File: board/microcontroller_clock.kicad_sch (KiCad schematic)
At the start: 3 parts, among them Y301 32768Hz

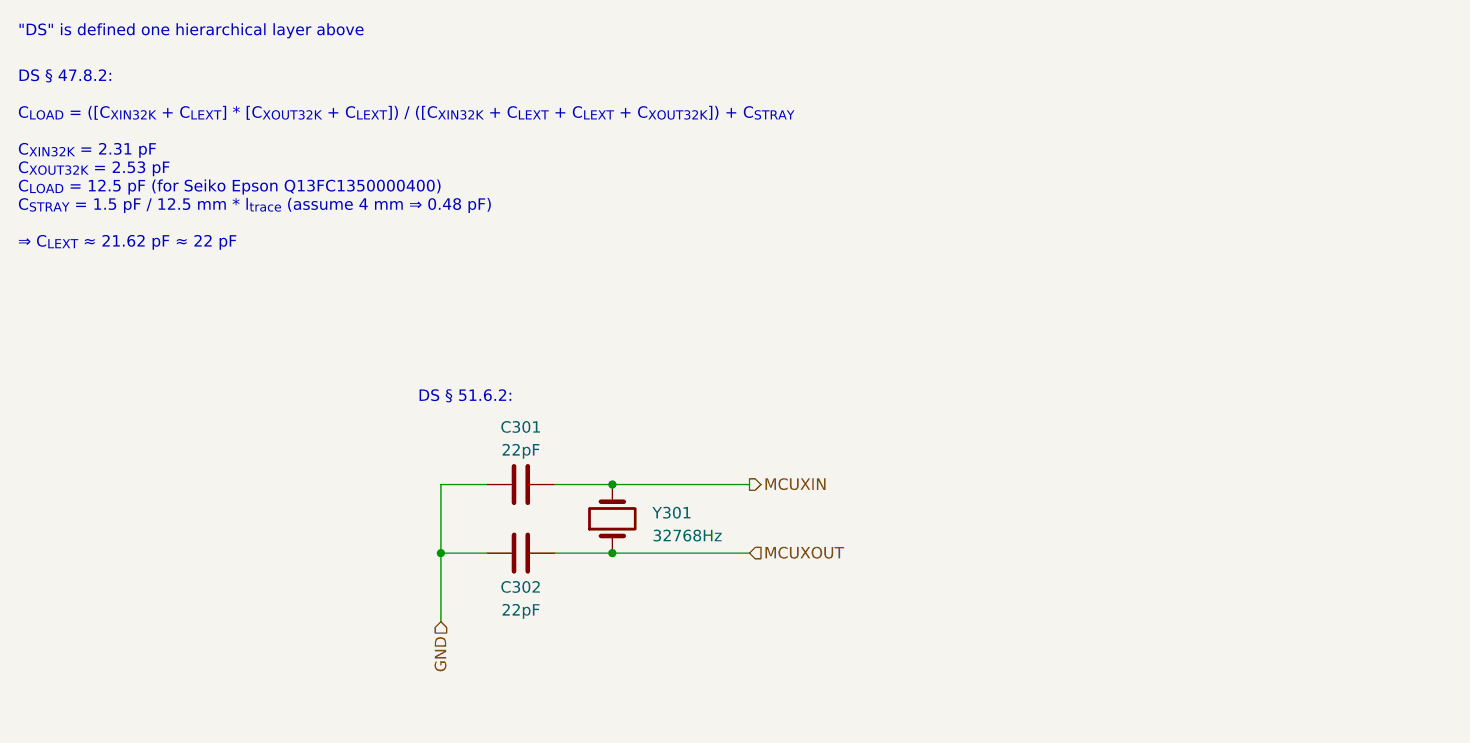
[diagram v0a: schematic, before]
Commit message: redo board with STM32G0B0CET
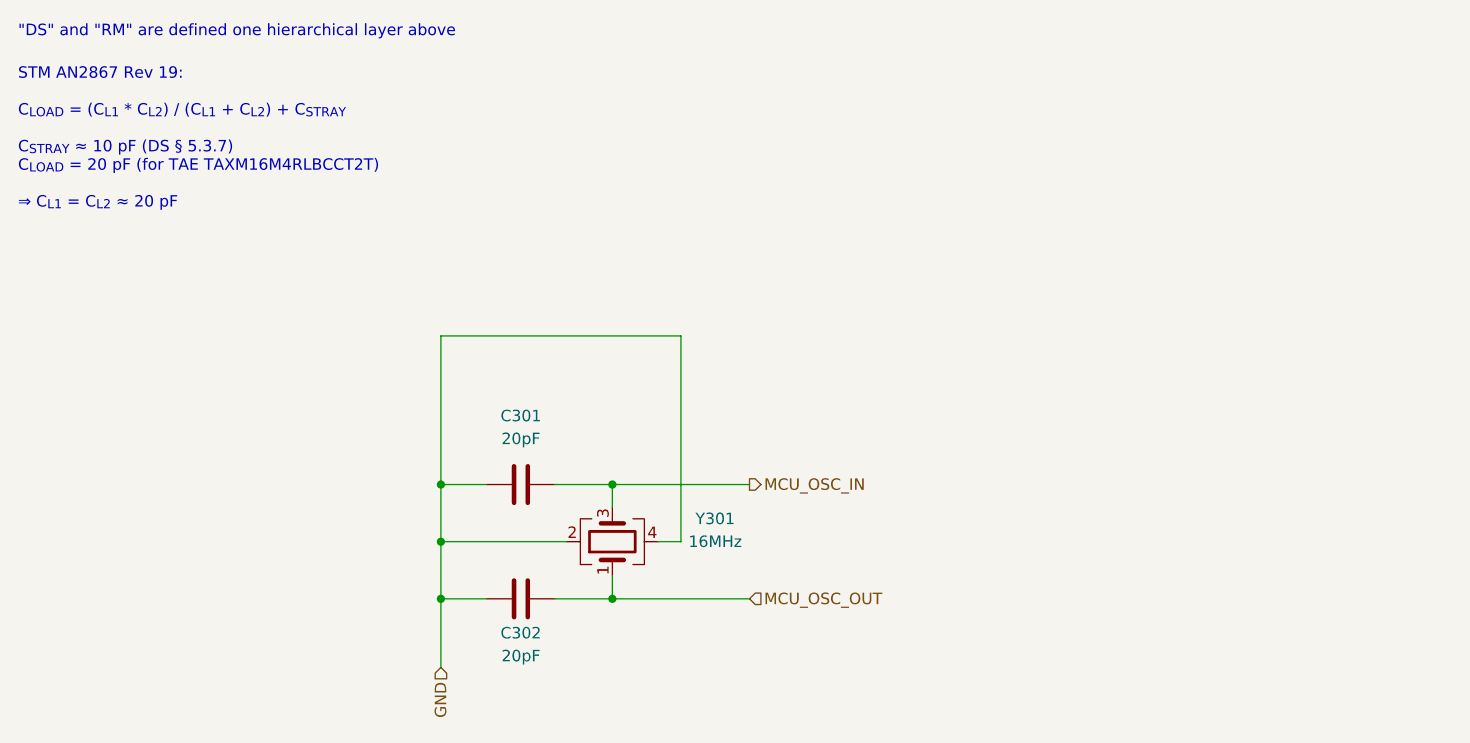
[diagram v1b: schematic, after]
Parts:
- C301, C302: value 22pF -> 20pF; LCSC C1555 -> C1554
- Y301: value 32768Hz -> 16MHz; footprint Crystal:Crystal_SMD_3215-2Pin_3.2x1.5mm -> Crystal:Crystal_SMD_3225-4Pin_3.2x2.5mm; symbol Device:Crystal -> Device:Crystal_GND24; LCSC C5120559 -> C164049
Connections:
- net GND: now also Y301.2, Y301.4
- net MCUXIN renamed MCU_OSC_IN
- net MCU_OSC_IN: now also Y301.3; no longer Y301.2
- net MCUXOUT renamed MCU_OSC_OUT
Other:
- note added: ""DS" and "RM" are defined one hierarchical layer above"
- note added: "STM AN2867 Rev 19: C_{LOAD} = (C_{L1} * C_{L2}) / (C_{L1} + C_{L2}) + C_{STRAY} C_{STRAY} ≈ 10 pF (DS § 5.3.7) C_{LOAD} = 20 pF (for TAE TAXM16M4RLBCCT2T) ⇒ C_{L1} = C_{L2} ≈ 20 pF"
- note removed: ""DS" is defined one hierarchical layer above"
- note removed: "DS § 47.8.2: C_{LOAD} = ([C_{XIN32K} + C_{LEXT}] * [C_{XOUT32K} + C_{LEXT}]) / ([C_{XIN32K} + C_{LEXT} + C_{LEXT} + C_{XOUT32K}]) + C_{STRAY} C_{XIN32K} = 2.31 pF C_{XOUT32K} = 2.53 pF C_{LOAD} = 12.5 pF (for Seiko Epson Q13FC1350000400) C_{STRAY} = 1.5 pF / 12.5 mm * l_{trace} (assume 4 mm ⇒ 0.48 pF) ⇒ C_{LEXT} ≈ 21.62 pF ≈ 22 pF"
- note removed: "DS § 51.6.2:"
- moved on the sheet: C302
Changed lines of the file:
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@@
 (kicad_sch (version 20230121) (generator eeschema)
   (paper "A4")
-  (junction (at 60.96 72.39) (diameter 0) (color 0 0 0 0)
+  (junction (at 60.96 77.47) (diameter 0) (color 0 0 0 0)
+  )
+  (junction (at 60.96 71.12) (diameter 0) (color 0 0 0 0)
   )
   (junction (at 80.01 64.77) (diameter 0) (color 0 0 0 0)
   )
-  (junction (at 80.01 72.39) (diameter 0) (color 0 0 0 0)
+  (junction (at 80.01 77.47) (diameter 0) (color 0 0 0 0)
+  )
+  (junction (at 60.96 64.77) (diameter 0) (color 0 0 0 0)
+  )
+  (wire (pts (xy 60.96 48.26) (xy 60.96 64.77))
+    (stroke (width 0) (type default))
+  )
+  (wire (pts (xy 60.96 71.12) (xy 60.96 77.47))
+    (stroke (width 0) (type default))
+  )
+  (wire (pts (xy 60.96 71.12) (xy 74.93 71.12))
+    (stroke (width 0) (type default))
+  )
+  (wire (pts (xy 87.63 71.12) (xy 85.09 71.12))
+    (stroke (width 0) (type default))
   )
   (wire (pts (xy 80.01 64.77) (xy 95.25 64.77))
     (stroke (width 0) (type default))
   )
-  (wire (pts (xy 60.96 72.39) (xy 60.96 80.01))
+  (wire (pts (xy 80.01 67.31) (xy 80.01 64.77))
     (stroke (width 0) (type default))
   )
-  (wire (pts (xy 73.66 72.39) (xy 80.01 72.39))
+  (wire (pts (xy 87.63 71.12) (xy 87.63 48.26))
     (stroke (width 0) (type default))
   )
-  (wire (pts (xy 80.01 72.39) (xy 95.25 72.39))
+  (wire (pts (xy 60.96 77.47) (xy 60.96 85.09))
     (stroke (width 0) (type default))
   )
-  (wire (pts (xy 60.96 72.39) (xy 66.04 72.39))
+  (wire (pts (xy 87.63 48.26) (xy 60.96 48.26))
+    (stroke (width 0) (type default))
+  )
+  (wire (pts (xy 73.66 77.47) (xy 80.01 77.47))
+    (stroke (width 0) (type default))
+  )
+  (wire (pts (xy 80.01 77.47) (xy 80.01 74.93))
+    (stroke (width 0) (type default))
+  )
+  (wire (pts (xy 80.01 77.47) (xy 95.25 77.47))
+    (stroke (width 0) (type default))
+  )
+  (wire (pts (xy 60.96 77.47) (xy 66.04 77.47))
     (stroke (width 0) (type default))
   )
@@
     (stroke (width 0) (type default))
   )
-  (wire (pts (xy 60.96 64.77) (xy 60.96 72.39))
+  (wire (pts (xy 60.96 64.77) (xy 60.96 71.12))
     (stroke (width 0) (type default))
   )
-  (text "DS § 51.6.2:" (at 58.42 55.88 0)
+  (text "STM AN2867 Rev 19:\n\nC_{LOAD} = (C_{L1} * C_{L2}) / (C_{L1} + C_{L2}) + C_{STRAY}\n\nC_{STRAY} ≈ 10 pF (DS § 5.3.7)\nC_{LOAD} = 20 pF (for TAE TAXM16M4RLBCCT2T)\n\n⇒ C_{L1} = C_{L2} ≈ 20 pF"
+    (at 13.97 34.29 0)
     (effects (font (size 1.27 1.27)) (justify left bottom))
   )
-  (text "DS § 47.8.2:\n\nC_{LOAD} = ([C_{XIN32K} + C_{LEXT}] * [C_{XOUT32K} + C_{LEXT}]) / ([C_{XIN32K} + C_{LEXT} + C_{LEXT} + C_{XOUT32K}]) + C_{STRAY}\n\nC_{XIN32K} = 2.31 pF\nC_{XOUT32K} = 2.53 pF\nC_{LOAD} = 12.5 pF (for Seiko Epson Q13FC1350000400)\nC_{STRAY} = 1.5 pF / 12.5 mm * l_{trace} (assume 4 mm ⇒ 0.48 pF)\n\n⇒ C_{LEXT} ≈ 21.62 pF ≈ 22 pF"
-    (at 13.97 38.735 0)
+  (text "\"DS\" and \"RM\" are defined one hierarchical layer above"
+    (at 13.97 15.24 0)
     (effects (font (size 1.27 1.27)) (justify left bottom))
   )
-  (text "\"DS\" is defined one hierarchical layer above" (at 13.97 15.24 0)
-    (effects (font (size 1.27 1.27)) (justify left bottom))
-  )
-  (hierarchical_label "MCUXIN" (shape output) (at 95.25 64.77 0) (fields_autoplaced)
+  (hierarchical_label "MCU_OSC_IN" (shape output) (at 95.25 64.77 0) (fields_autoplaced)
     (effects (font (size 1.27 1.27)) (justify left))
   )
-  (hierarchical_label "MCUXOUT" (shape input) (at 95.25 72.39 0) (fields_autoplaced)
+  (hierarchical_label "MCU_OSC_OUT" (shape input) (at 95.25 77.47 0) (fields_autoplaced)
     (effects (font (size 1.27 1.27)) (justify left))
   )
-  (hierarchical_label "GND" (shape input) (at 60.96 80.01 270) (fields_autoplaced)
+  (hierarchical_label "GND" (shape input) (at 60.96 85.09 270) (fields_autoplaced)
     (effects (font (size 1.27 1.27)) (justify right))
   )
-  (symbol (lib_id "Device:Crystal") (at 80.01 68.58 90) (unit 1)
-    (in_bom yes) (on_board yes) (dnp no) (fields_autoplaced)
-    (property "Reference" "Y301" (at 84.455 67.945 90)
-      (effects (font (size 1.27 1.27)) (justify right))
+  (symbol (lib_id "Device:Crystal_GND24") (at 80.01 71.12 90) (unit 1)
+    (in_bom yes) (on_board yes) (dnp no)
+    (property "Reference" "Y301" (at 91.44 68.58 90)
+      (effects (font (size 1.27 1.27)))
     )
-    (property "Value" "32768Hz" (at 84.455 70.485 90)
-      (effects (font (size 1.27 1.27)) (justify right))
+    (property "Value" "16MHz" (at 91.44 71.12 90)
+      (effects (font (size 1.27 1.27)))
     )
-    (property "Footprint" "Crystal:Crystal_SMD_3215-2Pin_3.2x1.5mm" (at 80.01 68.58 0)
+    (property "Footprint" "Crystal:Crystal_SMD_3225-4Pin_3.2x2.5mm" (at 80.01 71.12 0)
       (effects (font (size 1.27 1.27)) hide)
     )
-    (property "Datasheet" "~" (at 80.01 68.58 0)
+    (property "Datasheet" "~" (at 80.01 71.12 0)
       (effects (font (size 1.27 1.27)) hide)
     )
-    (property "LCSC" "C5120559" (at 80.01 68.58 0)
+    (property "LCSC" "C164049" (at 80.01 71.12 0)
       (effects (font (size 1.27 1.27)) hide)
     )
     (pin "1")
     (pin "2")
+    (pin "3")
+    (pin "4")
     (instances
       (project "bigredbutton"
@@
       )
       (project "enocean-heater-control"
-        (path "/5b6b7d93-1453-4f42-9207-d781d45a3d31/6e36ffc7-833c-490a-a419-d98d15ce7ac1/3e07dc11-3721-40d9-b0d4-7cbd77bafa21"
+        (path "/5b6b7d93-1453-4f42-9207-d781d45a3d31/6e36ffc7-833c-490a-a419-d98d15ce7ac1/ffec0bb5-2308-4547-a917-e412ae73decd"
           (reference "Y301") (unit 1)
         )
@@
   (symbol (lib_id "Device:C") (at 69.85 64.77 270) (unit 1)
     (in_bom yes) (on_board yes) (dnp no) (fields_autoplaced)
-    (property "Reference" "C301" (at 69.85 58.42 90)
+    (property "Reference" "C301" (at 69.85 57.15 90)
       (effects (font (size 1.27 1.27)))
     )
-    (property "Value" "22pF" (at 69.85 60.96 90)
+    (property "Value" "20pF" (at 69.85 59.69 90)
       (effects (font (size 1.27 1.27)))
     )
@@
       (effects (font (size 1.27 1.27)) hide)
     )
-    (property "LCSC" "C1555" (at 69.85 64.77 0)
+    (property "LCSC" "C1554" (at 69.85 64.77 0)
       (effects (font (size 1.27 1.27)) hide)
     )
@@
       )
       (project "enocean-heater-control"
-        (path "/5b6b7d93-1453-4f42-9207-d781d45a3d31/6e36ffc7-833c-490a-a419-d98d15ce7ac1/3e07dc11-3721-40d9-b0d4-7cbd77bafa21"
+        (path "/5b6b7d93-1453-4f42-9207-d781d45a3d31/6e36ffc7-833c-490a-a419-d98d15ce7ac1/ffec0bb5-2308-4547-a917-e412ae73decd"
           (reference "C301") (unit 1)
         )
@@
     )
   )
-  (symbol (lib_id "Device:C") (at 69.85 72.39 90) (unit 1)
+  (symbol (lib_id "Device:C") (at 69.85 77.47 90) (unit 1)
     (in_bom yes) (on_board yes) (dnp no)
-    (property "Reference" "C302" (at 69.85 76.2 90)
+    (property "Reference" "C302" (at 69.85 81.28 90)
       (effects (font (size 1.27 1.27)))
     )
-    (property "Value" "22pF" (at 69.85 78.74 90)
+    (property "Value" "20pF" (at 69.85 83.82 90)
       (effects (font (size 1.27 1.27)))
     )
-    (property "Footprint" "Capacitor_SMD:C_0402_1005Metric" (at 73.66 71.4248 0)
+    (property "Footprint" "Capacitor_SMD:C_0402_1005Metric" (at 73.66 76.5048 0)
       (effects (font (size 1.27 1.27)) hide)
     )
-    (property "Datasheet" "~" (at 69.85 72.39 0)
+    (property "Datasheet" "~" (at 69.85 77.47 0)
       (effects (font (size 1.27 1.27)) hide)
     )
-    (property "LCSC" "C1555" (at 69.85 72.39 0)
+    (property "LCSC" "C1554" (at 69.85 77.47 0)
       (effects (font (size 1.27 1.27)) hide)
     )
@@
       )
       (project "enocean-heater-control"
-        (path "/5b6b7d93-1453-4f42-9207-d781d45a3d31/6e36ffc7-833c-490a-a419-d98d15ce7ac1/3e07dc11-3721-40d9-b0d4-7cbd77bafa21"
+        (path "/5b6b7d93-1453-4f42-9207-d781d45a3d31/6e36ffc7-833c-490a-a419-d98d15ce7ac1/ffec0bb5-2308-4547-a917-e412ae73decd"
           (reference "C302") (unit 1)
         )
